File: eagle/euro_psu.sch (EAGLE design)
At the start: 40 parts, among them U1 POWER

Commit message: silkscreen draft
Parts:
- added U2: POWER, eurorack:POWER
- renumbered +5_ADJ1 to +5_ADJ, -12_ADJ1 to -12_ADJ, IC1 to LM317-1, IC2 to LM317-2, IC3 to LM337, LED1 to LED-12, LED2 to LED12, LED3 to LED5
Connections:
- net GNDA: now also U2.GND
- net N$10: now also U2.-12V
- net N$11: now also U2.+12V
- net N$12: now also U2.+5V

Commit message: rerouted with regulator protection diodes
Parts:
- removed U2: POWER, eurorack:POWER
- added D11, D12, D13: 1N4004, diode:1N4004
- R5, R6: value 4k7 -> 10k
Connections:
- net GNDA: no longer U2.GND
- net N$10: now also D13.C; no longer U2.-12V
- net N$11: now also D12.A; no longer U2.+12V
- net N$12: now also D11.A; no longer U2.+5V
- net N$3: now also D13.A
- net N$4: now also D11.C, D12.C
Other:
- moved on the sheet: +5_ADJ, C8, D1, D3, D7, D8, LED5, LM317-1, R3, R4

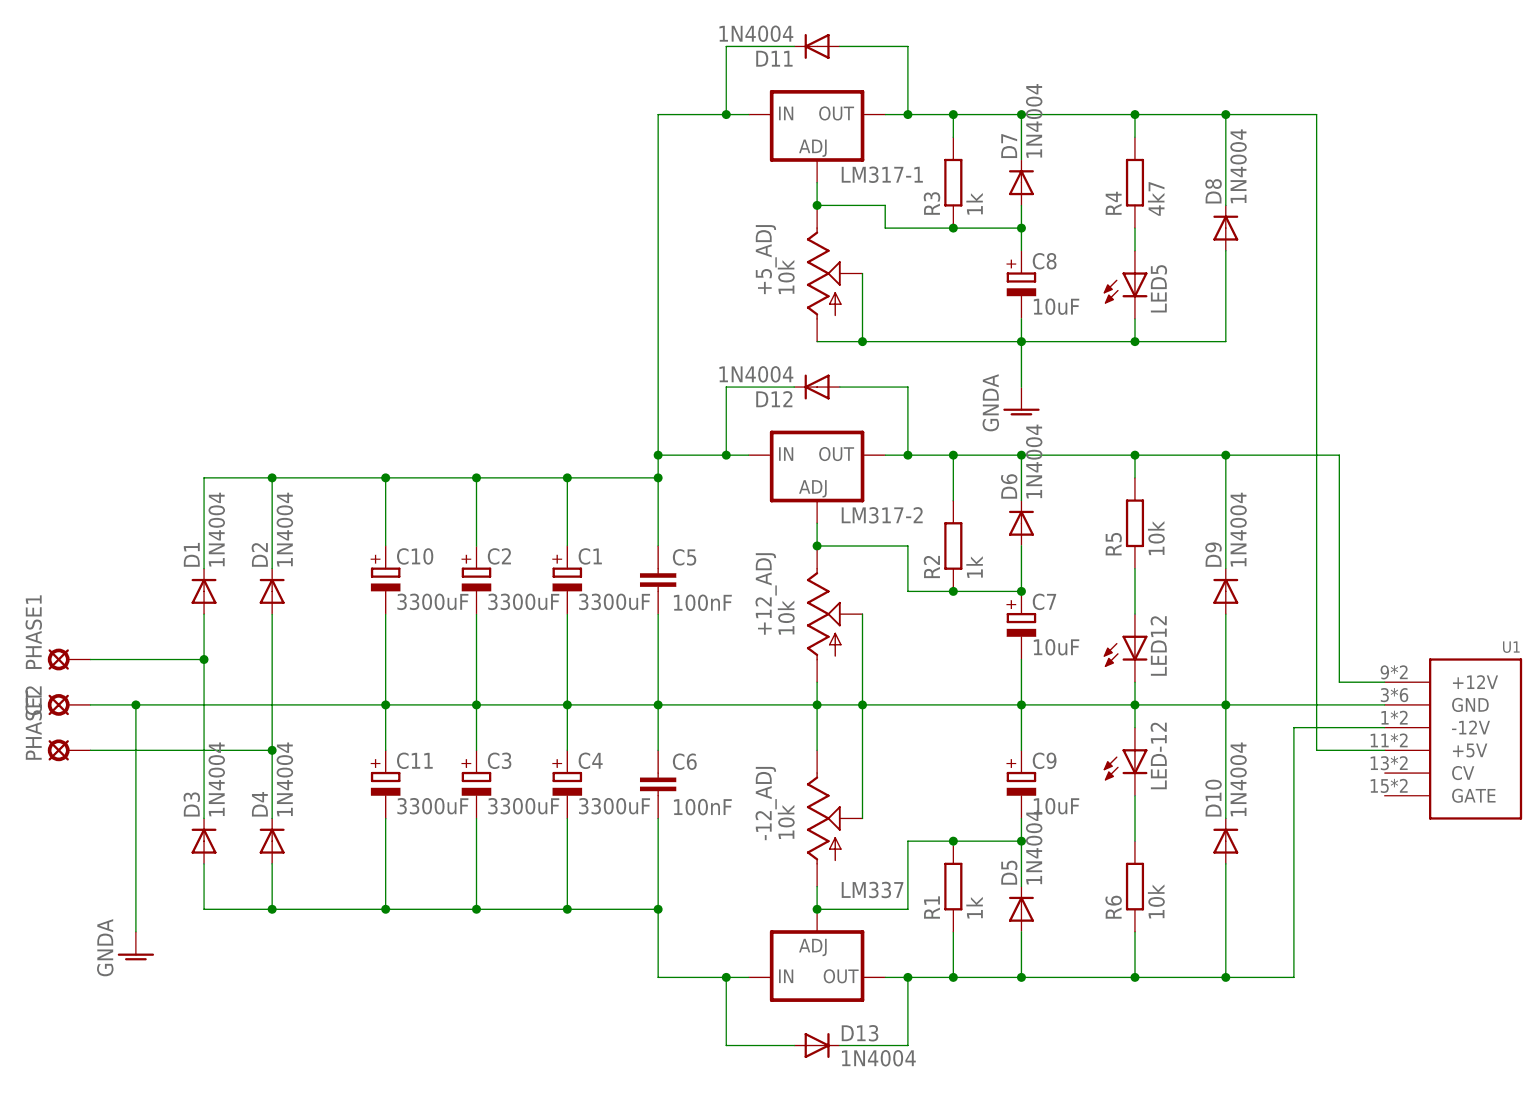
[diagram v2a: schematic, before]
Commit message: tweaked for more space behind the regulators
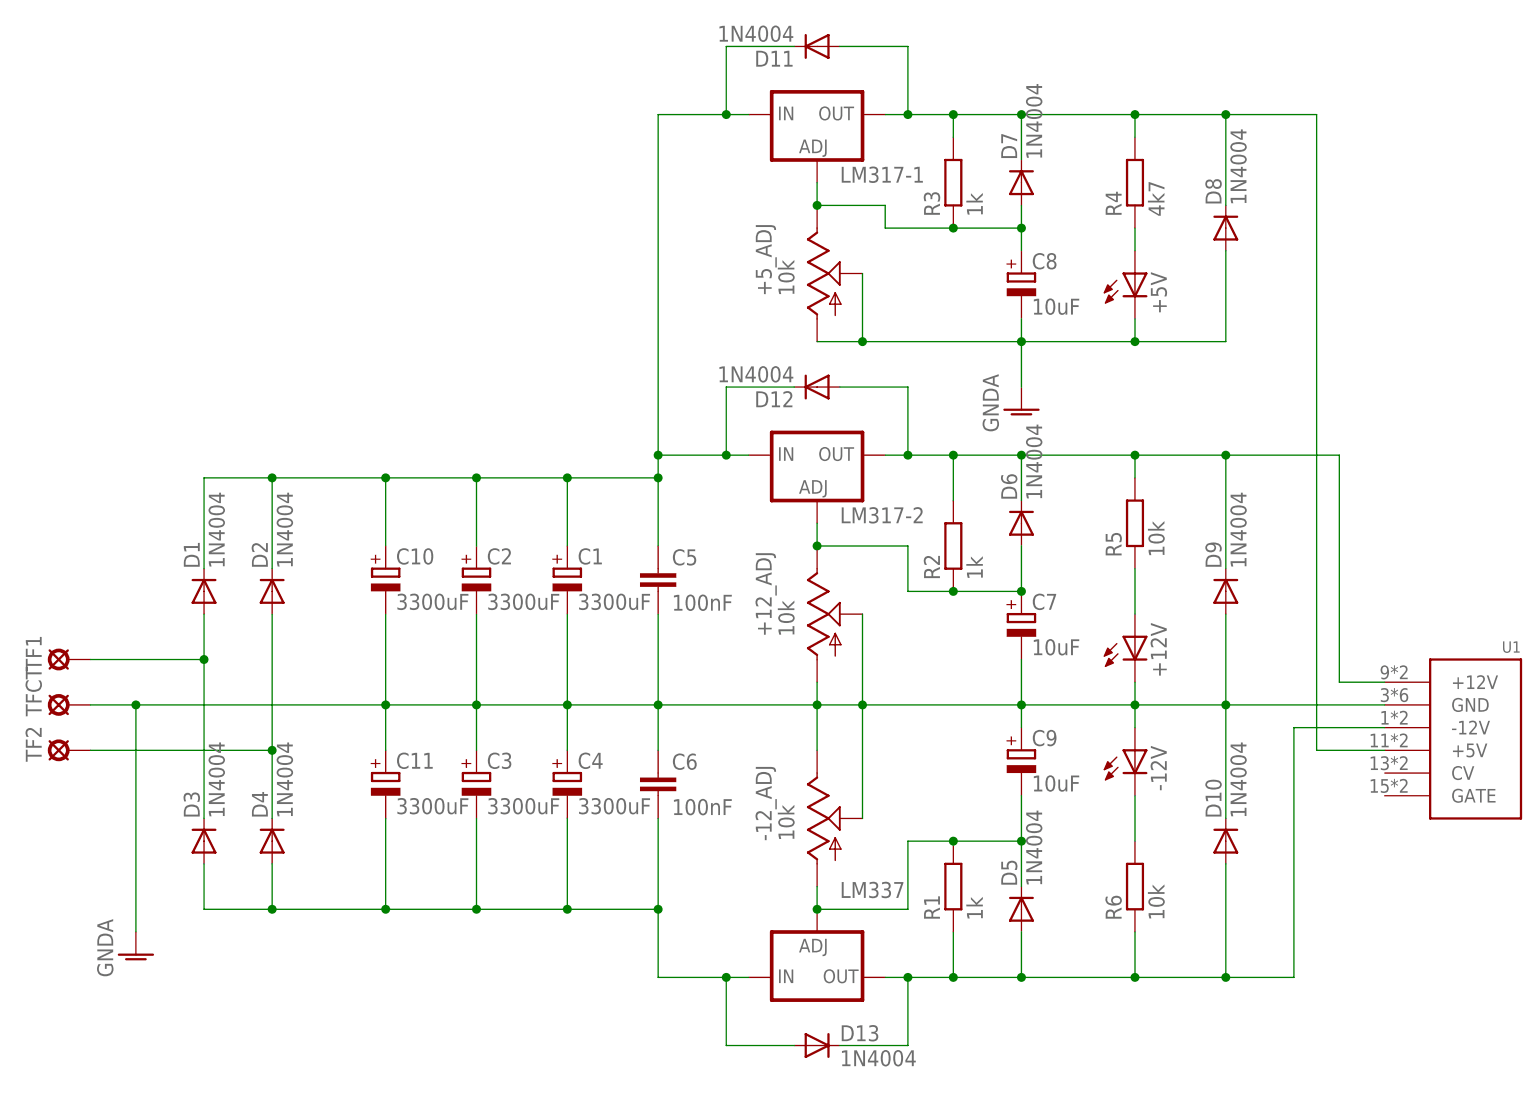
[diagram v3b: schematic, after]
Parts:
- renumbered CT to TFCT, LED-12 to -12V, LED12 to +12V, LED5 to +5V, PHASE1 to TF1, PHASE2 to TF2
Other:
- moved on the sheet: C9
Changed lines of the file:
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@@
 <?xml version="1.0" encoding="utf-8"?>
 <!DOCTYPE eagle SYSTEM "eagle.dtd">
-<eagle version="7.6.0">
+<eagle version="8.3.2">
 <drawing>
 <settings>
 <setting alwaysvectorfont="no"/>
+<setting keepoldvectorfont="yes"/>
 <setting verticaltext="up"/>
 </settings>
@@
 <part name="D3" library="diode" deviceset="1N4004" device=""/>
 <part name="D4" library="diode" deviceset="1N4004" device=""/>
-<part name="PHASE1" library="solpad" deviceset="SE14" device=""/>
-<part name="CT" library="solpad" deviceset="SE14" device=""/>
-<part name="PHASE2" library="solpad" deviceset="SE14" device=""/>
+<part name="TF1" library="solpad" deviceset="SE14" device=""/>
+<part name="TFCT" library="solpad" deviceset="SE14" device=""/>
+<part name="TF2" library="solpad" deviceset="SE14" device=""/>
 <part name="GND1" library="supply1" deviceset="GNDA" device=""/>
 <part name="C1" library="rcl" deviceset="CPOL-EU" device="E7.5-16" value="3300uF"/>
@@
 <part name="D6" library="diode" deviceset="1N4004" device=""/>
 <part name="D7" library="diode" deviceset="1N4004" device=""/>
-<part name="LED-12" library="led" deviceset="LED" device="5MM"/>
-<part name="LED12" library="led" deviceset="LED" device="5MM"/>
-<part name="LED5" library="led" deviceset="LED" device="5MM"/>
+<part name="-12V" library="led" deviceset="LED" device="5MM"/>
+<part name="+12V" library="led" deviceset="LED" device="5MM"/>
+<part name="+5V" library="led" deviceset="LED" device="5MM"/>
 <part name="R4" library="rcl" deviceset="R-EU_" device="0207/10" value="4k7"/>
 <part name="R5" library="rcl" deviceset="R-EU_" device="0207/10" value="10k"/>
@@
 <instance part="D3" gate="1" x="-193.04" y="99.06" rot="R90"/>
 <instance part="D4" gate="1" x="-185.42" y="99.06" rot="R90"/>
-<instance part="PHASE1" gate="1" x="-208.28" y="119.38" rot="R90"/>
-<instance part="CT" gate="1" x="-208.28" y="114.3" rot="R90"/>
-<instance part="PHASE2" gate="1" x="-208.28" y="109.22" rot="R90"/>
+<instance part="TF1" gate="1" x="-208.28" y="119.38" rot="R90"/>
+<instance part="TFCT" gate="1" x="-208.28" y="114.3" rot="R90"/>
+<instance part="TF2" gate="1" x="-208.28" y="109.22" rot="R90"/>
 <instance part="GND1" gate="1" x="-200.66" y="86.36"/>
 <instance part="C1" gate="G$1" x="-152.4" y="129.54"/>
@@
 <instance part="C7" gate="G$1" x="-101.6" y="124.46"/>
 <instance part="C8" gate="G$1" x="-101.6" y="162.56"/>
-<instance part="C9" gate="G$1" x="-101.6" y="106.68"/>
+<instance part="C9" gate="G$1" x="-101.6" y="109.22"/>
 <instance part="D5" gate="1" x="-101.6" y="91.44" rot="R90"/>
 <instance part="D6" gate="1" x="-101.6" y="134.62" rot="R90"/>
 <instance part="D7" gate="1" x="-101.6" y="172.72" rot="R90"/>
-<instance part="LED-12" gate="G$1" x="-88.9" y="109.22"/>
-<instance part="LED12" gate="G$1" x="-88.9" y="121.92"/>
-<instance part="LED5" gate="G$1" x="-88.9" y="162.56"/>
+<instance part="-12V" gate="G$1" x="-88.9" y="109.22"/>
+<instance part="+12V" gate="G$1" x="-88.9" y="121.92"/>
+<instance part="+5V" gate="G$1" x="-88.9" y="162.56"/>
 <instance part="R4" gate="G$1" x="-88.9" y="172.72" rot="R90"/>
 <instance part="R5" gate="G$1" x="-88.9" y="134.62" rot="R90"/>
@@
 <pinref part="D1" gate="1" pin="A"/>
 <wire x1="-193.04" y1="101.6" x2="-193.04" y2="119.38" width="0.1524" layer="91"/>
-<pinref part="PHASE1" gate="1" pin="MP"/>
+<pinref part="TF1" gate="1" pin="MP"/>
 <wire x1="-193.04" y1="119.38" x2="-193.04" y2="124.46" width="0.1524" layer="91"/>
 <wire x1="-205.74" y1="119.38" x2="-193.04" y2="119.38" width="0.1524" layer="91"/>
@@
 <pinref part="D4" gate="1" pin="C"/>
 <wire x1="-185.42" y1="124.46" x2="-185.42" y2="109.22" width="0.1524" layer="91"/>
-<pinref part="PHASE2" gate="1" pin="MP"/>
+<pinref part="TF2" gate="1" pin="MP"/>
 <wire x1="-185.42" y1="109.22" x2="-185.42" y2="101.6" width="0.1524" layer="91"/>
 <wire x1="-205.74" y1="109.22" x2="-185.42" y2="109.22" width="0.1524" layer="91"/>
@@
 <net name="GNDA" class="0">
 <segment>
-<pinref part="CT" gate="1" pin="MP"/>
+<pinref part="TFCT" gate="1" pin="MP"/>
 <pinref part="GND1" gate="1" pin="GNDA"/>
 <wire x1="-205.74" y1="114.3" x2="-200.66" y2="114.3" width="0.1524" layer="91"/>
@@
 <wire x1="-101.6" y1="114.3" x2="-119.38" y2="114.3" width="0.1524" layer="91"/>
 <pinref part="C9" gate="G$1" pin="+"/>
-<wire x1="-101.6" y1="109.22" x2="-101.6" y2="114.3" width="0.1524" layer="91"/>
+<wire x1="-101.6" y1="111.76" x2="-101.6" y2="114.3" width="0.1524" layer="91"/>
 <junction x="-101.6" y="114.3"/>
-<pinref part="LED12" gate="G$1" pin="C"/>
+<pinref part="+12V" gate="G$1" pin="C"/>
 <wire x1="-88.9" y1="116.84" x2="-88.9" y2="114.3" width="0.1524" layer="91"/>
 <wire x1="-88.9" y1="114.3" x2="-101.6" y2="114.3" width="0.1524" layer="91"/>
-<pinref part="LED-12" gate="G$1" pin="A"/>
+<pinref part="-12V" gate="G$1" pin="A"/>
 <wire x1="-88.9" y1="111.76" x2="-88.9" y2="114.3" width="0.1524" layer="91"/>
 <junction x="-88.9" y="114.3"/>
@@
 <wire x1="-101.6" y1="157.48" x2="-101.6" y2="154.94" width="0.1524" layer="91"/>
 <junction x="-101.6" y="154.94"/>
-<pinref part="LED5" gate="G$1" pin="C"/>
+<pinref part="+5V" gate="G$1" pin="C"/>
 <wire x1="-88.9" y1="157.48" x2="-88.9" y2="154.94" width="0.1524" layer="91"/>
 <wire x1="-88.9" y1="154.94" x2="-101.6" y2="154.94" width="0.1524" layer="91"/>
@@
 <pinref part="C9" gate="G$1" pin="-"/>
 <pinref part="D5" gate="1" pin="C"/>
-<wire x1="-101.6" y1="101.6" x2="-101.6" y2="99.06" width="0.1524" layer="91"/>
+<wire x1="-101.6" y1="104.14" x2="-101.6" y2="99.06" width="0.1524" layer="91"/>
 <wire x1="-101.6" y1="99.06" x2="-101.6" y2="93.98" width="0.1524" layer="91"/>
 <wire x1="-109.22" y1="99.06" x2="-101.6" y2="99.06" width="0.1524" layer="91"/>
@@
 <segment>
 <pinref part="R4" gate="G$1" pin="1"/>
-<pinref part="LED5" gate="G$1" pin="A"/>
+<pinref part="+5V" gate="G$1" pin="A"/>
 <wire x1="-88.9" y1="167.64" x2="-88.9" y2="165.1" width="0.1524" layer="91"/>
 </segment>
@@
 <segment>
 <pinref part="R6" gate="G$1" pin="2"/>
-<pinref part="LED-12" gate="G$1" pin="C"/>
+<pinref part="-12V" gate="G$1" pin="C"/>
 <wire x1="-88.9" y1="99.06" x2="-88.9" y2="104.14" width="0.1524" layer="91"/>
 </segment>
@@
 <net name="N$25" class="0">
 <segment>
-<pinref part="LED12" gate="G$1" pin="A"/>
+<pinref part="+12V" gate="G$1" pin="A"/>
 <pinref part="R5" gate="G$1" pin="1"/>
 <wire x1="-88.9" y1="124.46" x2="-88.9" y2="129.54" width="0.1524" layer="91"/>
